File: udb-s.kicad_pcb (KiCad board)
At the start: 2 copper layers, 13 x 15.1 mm, 9 parts, among them J1 TYPE-C-31-M-12, J2 Conn_01x04, J3 Conn_01x04, U1 TPD4E05U06DQAR

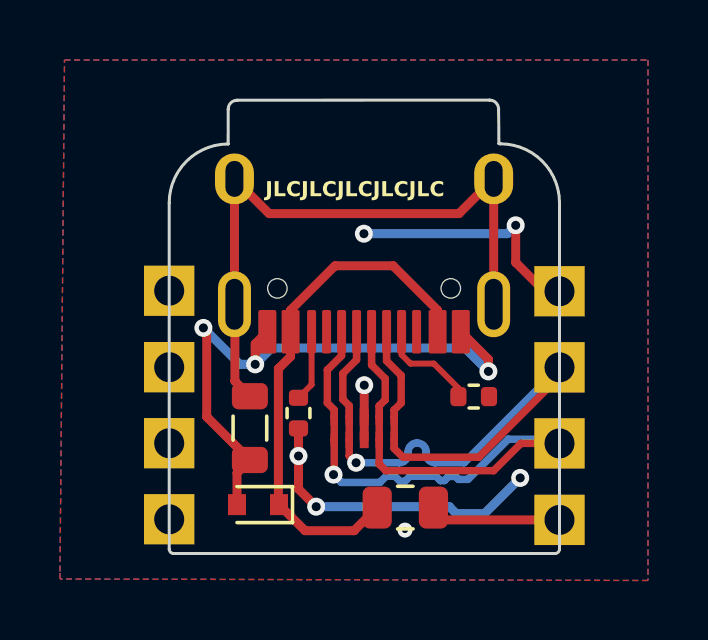
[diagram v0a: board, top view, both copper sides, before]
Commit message: Fix inconsistent alignment
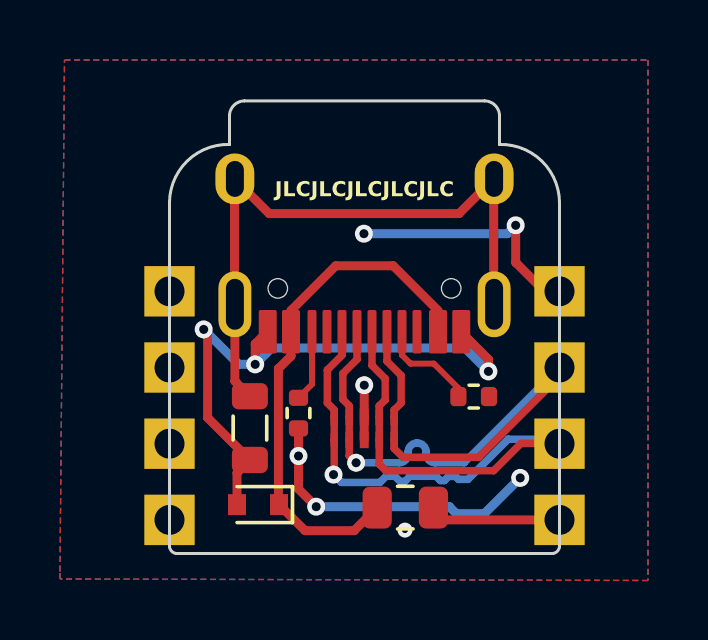
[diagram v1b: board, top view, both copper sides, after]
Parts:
- moved J3 4.18 mm to (122.8, 87.0), turned to 180 degrees
- moved J2 4.16 mm to (135.8, 87.0)
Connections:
- J3 pad 1: unconnected-(J3-Pad1) -> (no net)
- J3 pad 2: unconnected-(J3-Pad2) -> (no net)
- J3 pad 3: unconnected-(J3-Pad3) -> (no net)
- J3 pad 4: unconnected-(J3-Pad4) -> (no net)
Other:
- outline, holes or cut-outs redrawn
